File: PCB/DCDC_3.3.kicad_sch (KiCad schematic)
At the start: 19 parts, among them Q4 2N7002, U11 LV2842XLVDDCR

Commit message: corrections and todos
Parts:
- R3: now not fitted
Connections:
- net at R40.2, R48.1, R49.2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: no longer Q4.3 (D)
- no-connect marks 0 -> 2
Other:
- note added: "Calculate resistors for undervoltage cutout: I_{1} = 1uA I_{Hyst}=3uA V_{Ena} = 1.25V (1.05...1.38) There is a diode in series D1_V{F}_ON = 0.8 D1_V{F}_OFF = 0.5 Assume typical V_{Ena} = 1.2V: R1 = (V_{start} - V_{stop} - D1_V{F}_ON)/I_{Hyst} R1 = (11V - 10) / 3uA = 1 MOhm, but assume 100kOhm and add hysteresis from the output R2 = V_{Ena} / ((V_{start}-D1_V{F}_OFF - V_{Ena})/R1+I_{1}) R2_{rounde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"
- note added: "Remove R3 to force always enable"
- note added: "provides extra hysteresis"
- note added: "severed - still inactive"
- note added: "todo: R3+R49 = 8.2k+4.7k;"
- note added: "todo: add 56k Mosfet pull down."
- note removed: "Calculate resistors for undervoltage cutout: I_{1} = 1uA I_{Hyst}=3uA V_{Ena} = 1.25V (1.05...1.38) Assume typical V_{Ena} = 1.2V: R1 = (V_{start} - V_{stop})/I_{Hyst} R1 = (11V - 9) / 3uA = 100kOhm // don't care about hysteresis anyway R2 = V_{Ena} / ((V_{start} - V_{Ena})/R1+I_{1}) R2_{rounded} = 1.2V / ((7.1V-1.2V)/100kOhm + 1uA) = 20kOhm There is a diode in series D1_V{F}_ON = 0.8 D1_V{F}_OFF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"
- note removed: "Remove R49 to force always enable"
- moved on the sheet: Q4
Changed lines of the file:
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@@
+		)
+	)
+	(text "provides\nextra hysteresis"
+		(exclude_from_sim no)
+		(at 129.032 133.35 0)
+		(effects
+			(font
+				(size 1.27 1.27)
+			)
+		)
+	)
+	(text "todo:\nadd 56k Mosfet pull down."
+		(exclude_from_sim no)
+		(at 80.264 147.828 0)
+		(effects
+			(font
+				(size 1.27 1.27)
+				(color 255 0 255 1)
+			)
+			(justify left)
 		)
 	)
@@
 		)
 	)
+	(text "severed\n- still inactive"
+		(exclude_from_sim no)
+		(at 92.71 132.334 0)
+		(effects
+			(font
+				(size 1.27 1.27)
+				(italic yes)
+				(color 255 0 255 1)
+			)
+			(justify left)
+		)
+	)
 	(text "R1"
 		(exclude_from_sim no)
@@
 		)
 	)
-	(text "Calculate resistors for undervoltage cutout:\nI_{1} = 1uA\nI_{Hyst}=3uA\nV_{Ena} = 1.25V  (1.05...1.38)\n\nAssume typical V_{Ena} = 1.2V:\nR1 = (V_{start} - V_{stop})/I_{Hyst}\nR1 = (11V - 9) / 3uA = 100kOhm // don't care about hysteresis anyway\nR2 = V_{Ena} / ((V_{start} - V_{Ena})/R1+I_{1})\nR2_{rounded} = 1.2V / ((7.1V-1.2V)/100kOhm + 1uA) = 20kOhm\n\nThere is a diode in series\nD1_V{F}_ON = 0.8\nD1_V{F}_OFF = 0.5\nso actual threshold is:\nV_{stop_real} = V_{stop}+D1_V{F}_ON\nV_{start_real} = V_{start}+D1_V{F}_OFF\nV_{stop_real} = 6.5 + 0.8 = 7.3V\nV_{start_real} = 7.1 + 0.4 = 7.5V"
-		(exclude_from_sim no)
-		(at 25.654 176.276 0)
+	(text "Calculate resistors for undervoltage cutout:\nI_{1} = 1uA\nI_{Hyst}=3uA\nV_{Ena} = 1.25V  (1.05...1.38)\nThere is a diode in series\nD1_V{F}_ON = 0.8\nD1_V{F}_OFF = 0.5\n\nAssume typical V_{Ena} = 1.2V:\nR1 = (V_{start} - V_{stop} - D1_V{F}_ON)/I_{Hyst}\nR1 = (11V - 10) / 3uA = 1 MOhm, but assume 100kOhm and add hysteresis from the output\nR2 = V_{Ena} / ((V_{start}-D1_V{F}_OFF - V_{Ena})/R1+I_{1})\nR2_{rounded} = 1.2V / ((12V-0.5V-1.2V)/100kOhm + 1uA) = 11.4kOhm\n\nNeeds to be tuned in real world"
+		(exclude_from_sim no)
+		(at 23.876 182.88 0)
 		(effects
 			(font
@@
 		)
 	)
-	(text "Remove R49 to force always enable"
-		(exclude_from_sim no)
-		(at 102.616 172.974 0)
+	(text "Remove R3 to force always enable"
+		(exclude_from_sim no)
+		(at 113.792 156.972 0)
 		(effects
 			(font
@@
 		)
 	)
+	(text "todo:\nR3+R49 = 8.2k+4.7k;"
+		(exclude_from_sim no)
+		(at 115.062 144.272 0)
+		(effects
+			(font
+				(size 1.27 1.27)
+				(color 255 0 255 1)
+			)
+			(justify left)
+		)
+	)
 	(junction
 		(at 210.82 83.82)
@@
 		(color 0 0 0 0)
 	)
+	(no_connect
+		(at 102.87 129.54)
+	)
+	(no_connect
+		(at 99.06 129.54)
+	)
 	(wire
 		(pts
@@
 	(wire
 		(pts
-			(xy 88.9 138.43) (xy 92.71 138.43)
+			(xy 102.87 129.54) (xy 109.22 129.54)
+		)
+		(stroke
+			(width 0)
+			(type default)
+		)
+	)
+	(wire
+		(pts
+			(xy 78.74 138.43) (xy 82.55 138.43)
 		)
 		(stroke
@@
 	(wire
 		(pts
-			(xy 100.33 129.54) (xy 100.33 133.35)
+			(xy 90.17 129.54) (xy 90.17 133.35)
 		)
 		(stroke
@@
 	(wire
 		(pts
-			(xy 100.33 143.51) (xy 100.33 147.32)
+			(xy 90.17 143.51) (xy 90.17 147.32)
 		)
 		(stroke
@@
 	(wire
 		(pts
-			(xy 100.33 129.54) (xy 109.22 129.54)
-		)
-		(stroke
-			(width 0)
-			(type default)
-		)
-	)
-	(wire
-		(pts
-			(xy 100.33 147.32) (xy 109.22 147.32)
+			(xy 90.17 147.32) (xy 109.22 147.32)
 		)
 		(stroke
@@
 		(pts
 			(xy 124.46 129.54) (xy 129.54 129.54)
+		)
+		(stroke
+			(width 0)
+			(type default)
+		)
+	)
+	(wire
+		(pts
+			(xy 90.17 129.54) (xy 99.06 129.54)
 		)
 		(stroke
@@
 	(hierarchical_label "~{Enable}"
 		(shape input)
-		(at 88.9 138.43 180)
+		(at 78.74 138.43 180)
 		(effects
 			(font
@@
 		(in_bom yes)
 		(on_board yes)
-		(dnp no)
+		(dnp yes)
 		(property "Reference" "R3"
 			(at 111.76 142.24 90)
@@
 	(symbol
 		(lib_id "Transistor_FET:2N7002")
-		(at 97.79 138.43 0)
+		(at 87.63 138.43 0)
 		(unit 1)
 		(exclude_from_sim no)
@@
 		(dnp no)
 		(property "Reference" "Q4"
-			(at 94.488 135.89 0)
+			(at 84.328 135.89 0)
 			(effects
 				(font
@@
 		)
 		(property "Value" "2N7002"
-			(at 89.916 141.732 0)
+			(at 79.756 141.732 0)
 			(effects
 				(font
@@
 		)
 		(property "Footprint" "Package_TO_SOT_SMD:SOT-23"
-			(at 102.87 140.335 0)
+			(at 92.71 140.335 0)
 			(effects
 				(font
@@
 		)
 		(property "Datasheet" "https://datasheet.lcsc.com/lcsc/2304140030_Jiangsu-Changjing-Electronics-Technology-Co---Ltd--2N7002_C8545.pdf"
-			(at 97.79 138.43 0)
+			(at 87.63 138.43 0)
 			(effects
 				(font
@@
 		)
 		(property "Description" ""
-			(at 97.79 138.43 0)
+			(at 87.63 138.43 0)
 			(effects
 				(font
@@
 		)
 		(property "LCSC" "C8545"
-			(at 97.79 138.43 0)
-			(effects
-				(font
+			(at 87.63 138.43 0)
+			(effects
+				(font

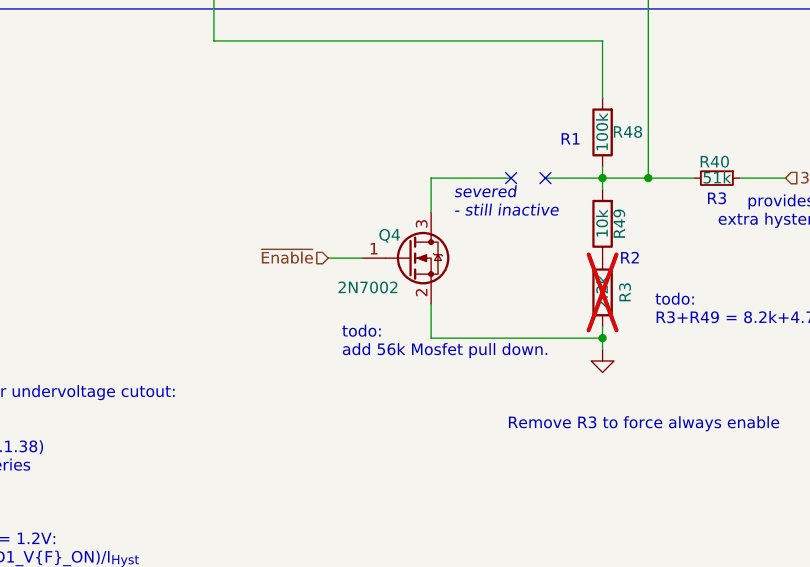
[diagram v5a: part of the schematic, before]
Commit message: Added dcdc shutdown mosfet pulldown
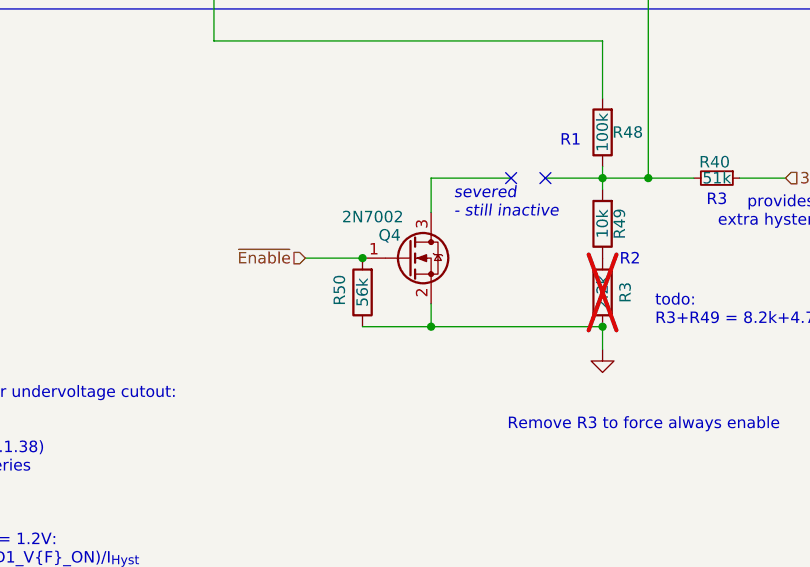
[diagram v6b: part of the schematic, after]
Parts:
- added R50: 56k, Resistor_SMD:R_0402_1005Metric, symbol Device:R
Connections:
- net GND: now also R50.1
- net ~{Enable}: now also R50.2
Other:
- note removed: "todo: add 56k Mosfet pull down."
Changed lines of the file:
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@@
-		)
-	)
-	(text "todo:\nadd 56k Mosfet pull down."
-		(exclude_from_sim no)
-		(at 80.264 147.828 0)
-		(effects
-			(font
-				(size 1.27 1.27)
-				(color 255 0 255 1)
-			)
-			(justify left)
 		)
 	)
@@
 	)
 	(junction
+		(at 82.55 138.43)
+		(diameter 0)
+		(color 0 0 0 0)
+	)
+	(junction
 		(at 182.88 83.82)
 		(diameter 0)
@@
 	)
 	(junction
-		(at 177.8 83.82)
+		(at 109.22 146.05)
 		(diameter 0)
 		(color 0 0 0 0)
 	)
 	(junction
-		(at 109.22 147.32)
+		(at 177.8 83.82)
 		(diameter 0)
 		(color 0 0 0 0)
@@
 	)
 	(junction
+		(at 90.17 146.05)
+		(diameter 0)
+		(color 0 0 0 0)
+	)
+	(junction
 		(at 162.56 83.82)
 		(diameter 0)
@@
 	(wire
 		(pts
-			(xy 78.74 138.43) (xy 82.55 138.43)
+			(xy 76.2 138.43) (xy 82.55 138.43)
 		)
 		(stroke
@@
 	(wire
 		(pts
-			(xy 90.17 143.51) (xy 90.17 147.32)
+			(xy 109.22 146.05) (xy 109.22 148.59)
+		)
+		(stroke
+			(width 0)
+			(type default)
+		)
+	)
+	(wire
+		(pts
+			(xy 90.17 143.51) (xy 90.17 146.05)
 		)
 		(stroke
@@
 	(wire
 		(pts
+			(xy 82.55 146.05) (xy 90.17 146.05)
+		)
+		(stroke
+			(width 0)
+			(type default)
+		)
+	)
+	(wire
+		(pts
 			(xy 114.3 86.36) (xy 114.3 129.54)
 		)
@@
 	(wire
 		(pts
-			(xy 109.22 147.32) (xy 109.22 148.59)
-		)
-		(stroke
-			(width 0)
-			(type default)
-		)
-	)
-	(wire
-		(pts
-			(xy 109.22 146.05) (xy 109.22 147.32)
-		)
-		(stroke
-			(width 0)
-			(type default)
-		)
-	)
-	(wire
-		(pts
 			(xy 71.12 81.28) (xy 83.82 81.28)
 		)
@@
 	(wire
 		(pts
-			(xy 90.17 147.32) (xy 109.22 147.32)
+			(xy 90.17 146.05) (xy 109.22 146.05)
 		)
 		(stroke
@@
 	(hierarchical_label "~{Enable}"
 		(shape input)
-		(at 78.74 138.43 180)
+		(at 76.2 138.43 180)
 		(effects
 			(font
@@
 	)
 	(symbol
+		(lib_id "Device:R")
+		(at 82.55 142.24 180)
+		(unit 1)
+		(exclude_from_sim no)
+		(in_bom yes)
+		(on_board yes)
+		(dnp no)
+		(property "Reference" "R50"
+			(at 80.01 141.986 90)
+			(effects
+				(font
+					(size 1.27 1.27)
+				)
+			)
+		)
+		(property "Value" "56k"
+			(at 82.55 142.24 90)
+			(effects
+				(font
+					(size 1.27 1.27)
+				)
+			)
+		)
+		(property "Footprint" "Resistor_SMD:R_0402_1005Metric"
+			(at 84.328 142.24 90)
+			(effects
+				(font
+					(size 1.27 1.27)
+				)
+				(hide yes)
+			)
+		)
+		(property "Datasheet" "~"
+			(at 82.55 142.24 0)
+			(effects
+				(font
+					(size 1.27 1.27)
+				)
+				(hide yes)
+			)
+		)
+		(property "Description" ""
+			(at 82.55 142.24 0)
+			(effects
+				(font
+					(size 1.27 1.27)
+				)
+				(hide yes)
+			)
+		)
+		(property "LCSC" "C25796"
+			(at 84.455 142.24 0)
+			(effects
+				(font
+					(size 1.27 1.27)
+				)
+				(hide yes)
+			)
+		)
+		(pin "1"
+		)
+		(pin "2"
+		)
+		(instances
+			(project "StepperServoCAN"
+				(path "/92dad13e-412a-43d4-9260-9087579302b1/82f027ad-2d00-453d-ab1c-0ba3b5cb1ef7"
+					(reference "R50")
+					(unit 1)
+				)
+			)
+		)
+	)
+	(symbol
 		(lib_id "Device:C_Small")
 		(at 177.8 86.36 0)
@@
 		)
 		(property "Value" "2N7002"
-			(at 79.756 141.732 0)
-			(effects
-				(font
+			(at 80.264 133.858 0)
+			(effects
+				(font
